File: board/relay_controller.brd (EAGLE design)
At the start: 70 x 50 mm, 53 parts, among them IC1 STM32F103C8T, IC3 AT24C, X1 RJ45-8L21-S, X2 RJ45-8L21-S

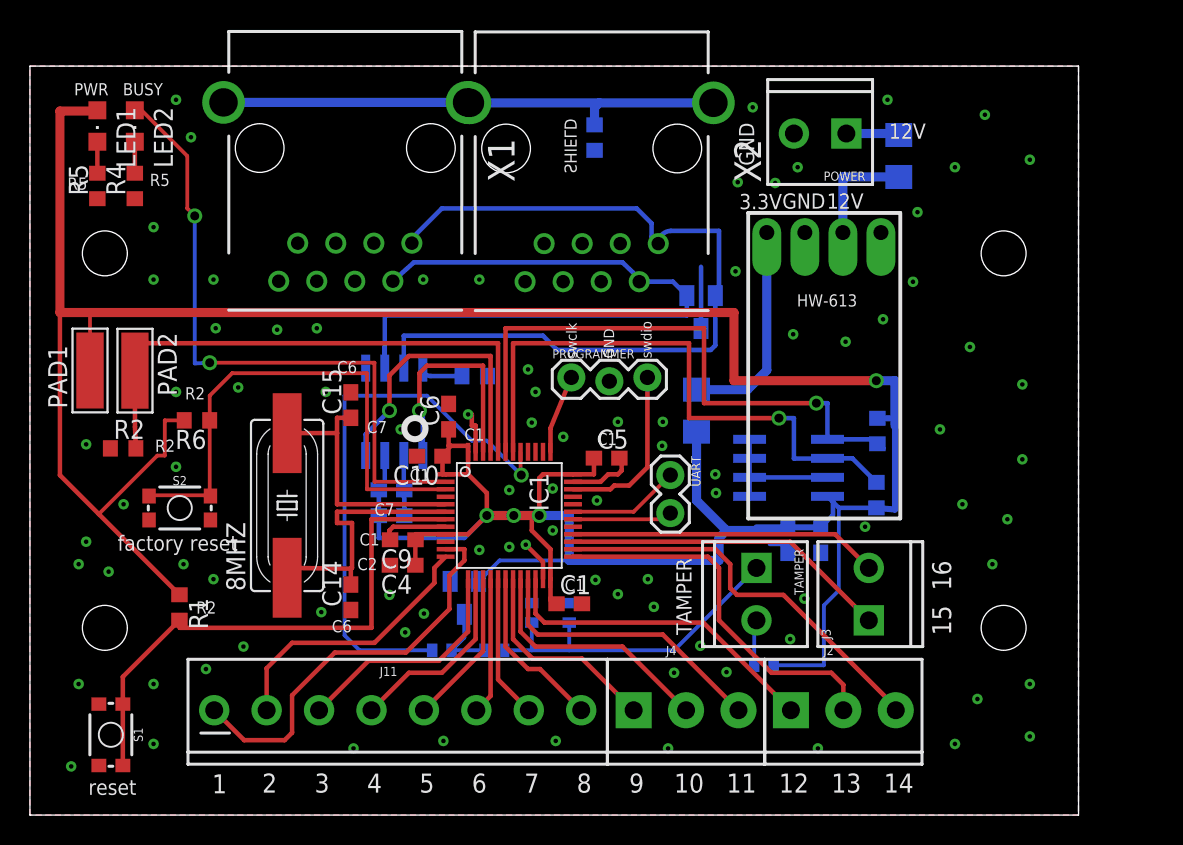
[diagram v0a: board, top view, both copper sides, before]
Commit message: add 3.3v output for relay board
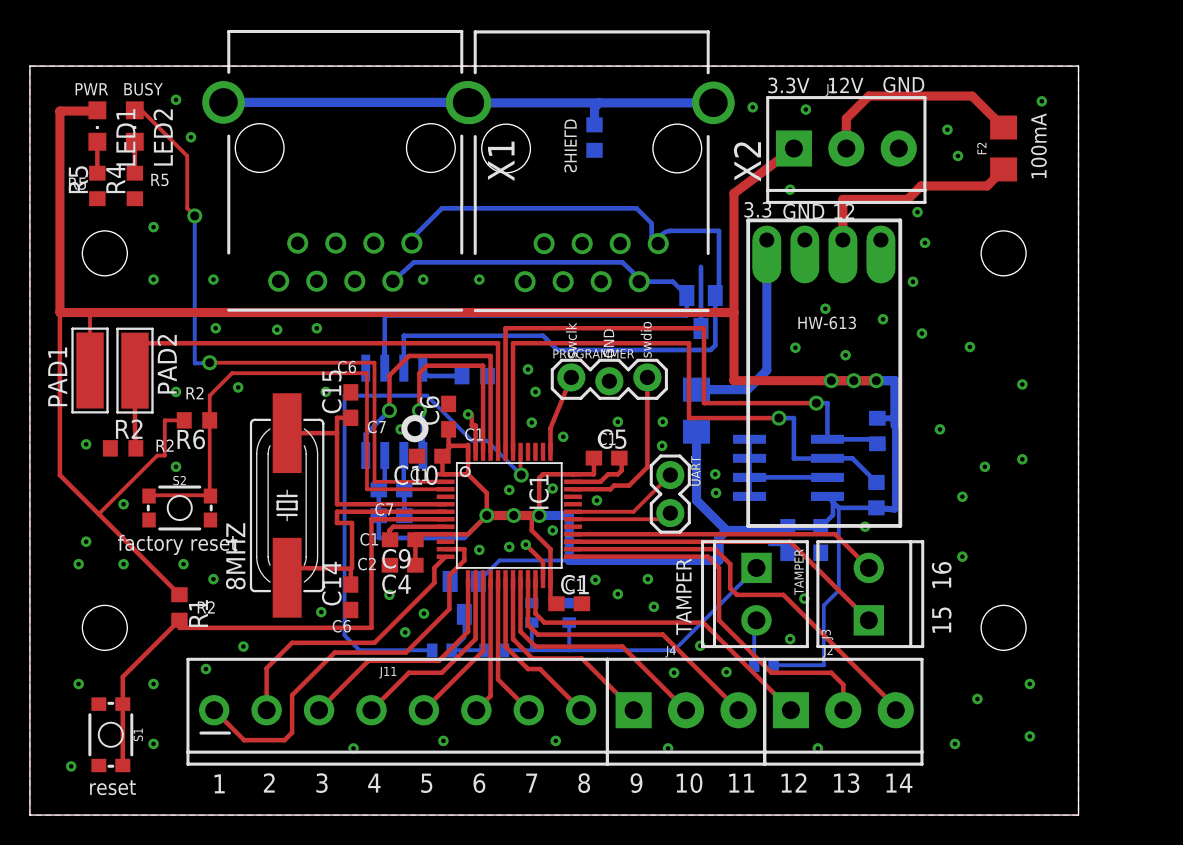
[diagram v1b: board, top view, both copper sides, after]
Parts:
- removed POWER: (no value), SparkFun-Connectors:SCREWTERMINAL-3.5MM-2
- added J1: (no value), SparkFun-Connectors:SCREWTERMINAL-3.5MM-3
- moved F2 7.02 mm to (65.0, 44.5), flipped to the top
- moved U$1 0.50 mm to (53.0, 29.5)
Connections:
- net +3V3: now also J1.1
- net GND: now also J1.3; no longer POWER.2
- net N$4: now also J1.2; no longer POWER.1
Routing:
- net +3V3: track 239.8 -> 255.8 mm, vias 4 -> 6
- net N$4: track 3.60 -> 14.0 mm
- net +12V: track 7.44 -> 14.3 mm
- net N$3: track 14.4 -> 13.9 mm
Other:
- board text added: "100mA"
- board text added: "3.3"
- board text added: "relay controller 2020.06.07 v1.1"
- board text removed: "2020.05.07 v1.0"
- board text removed: "50mA"

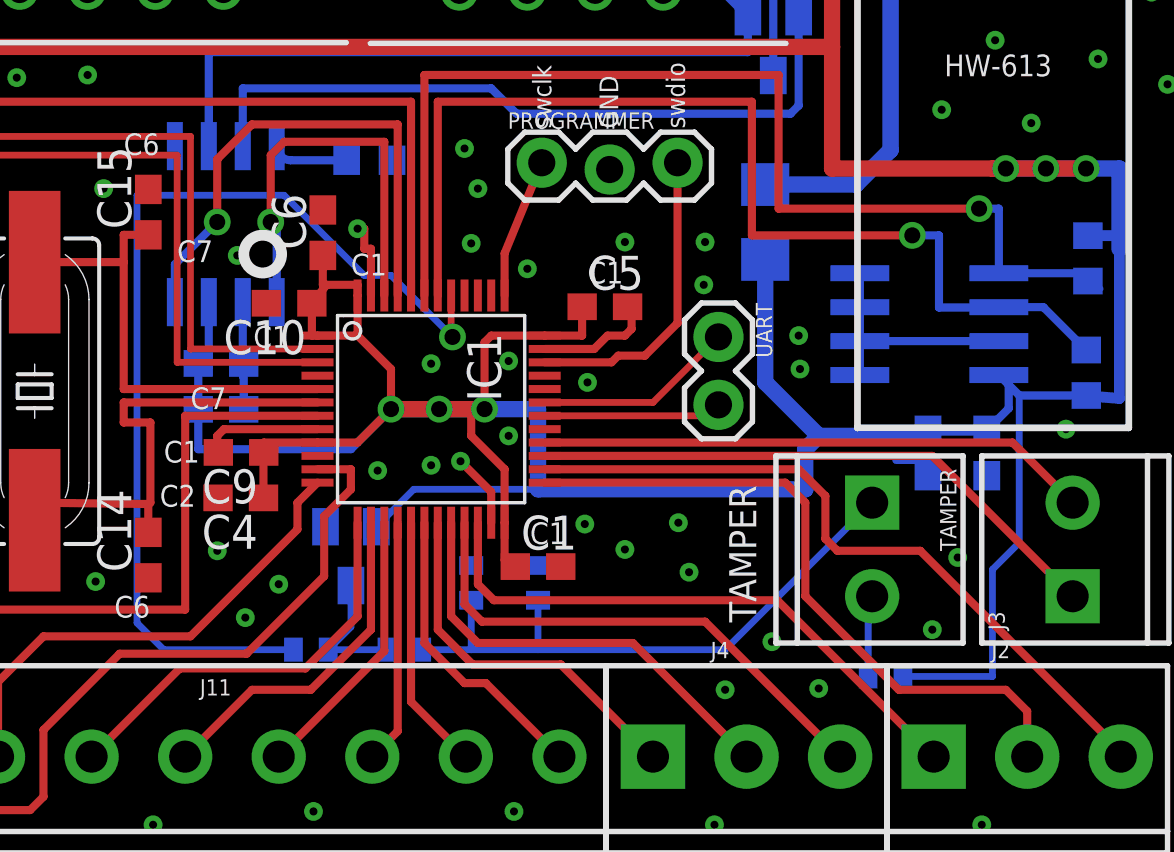
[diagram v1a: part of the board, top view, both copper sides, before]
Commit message: add 3.3v output
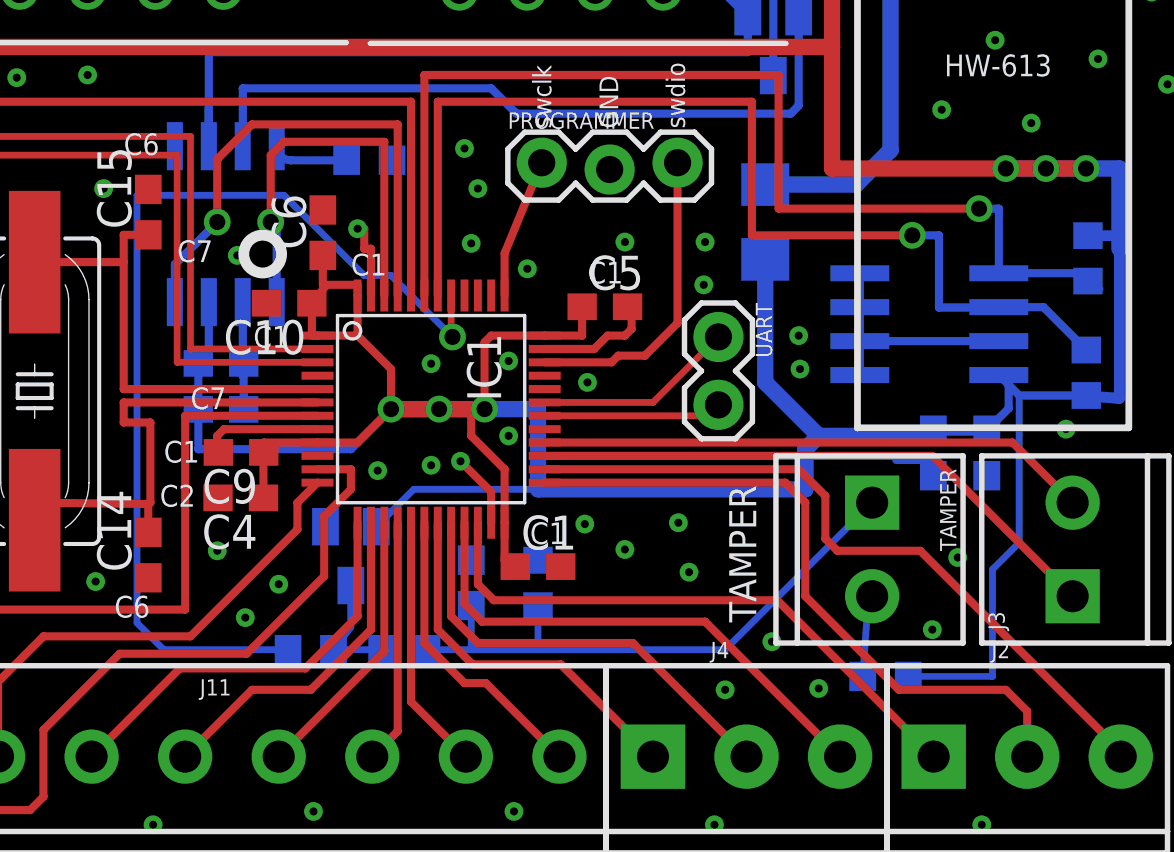
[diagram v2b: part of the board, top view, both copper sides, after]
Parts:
- C11: device eagle-ltspice:C0402 -> eagle-ltspice:C0603
- R59, R60, R61, R62: device rcl:R0402 -> rcl:R0603
- moved C2 0.20 mm to (50.8, 18.4)
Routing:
- net N$5: track 22.8 -> 22.2 mm
- net ASDASD: track 4.95 -> 4.42 mm
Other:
- board text added: "C13"
- board text removed: "C9"
- board text removed: "R16"
- board text removed: "R17"

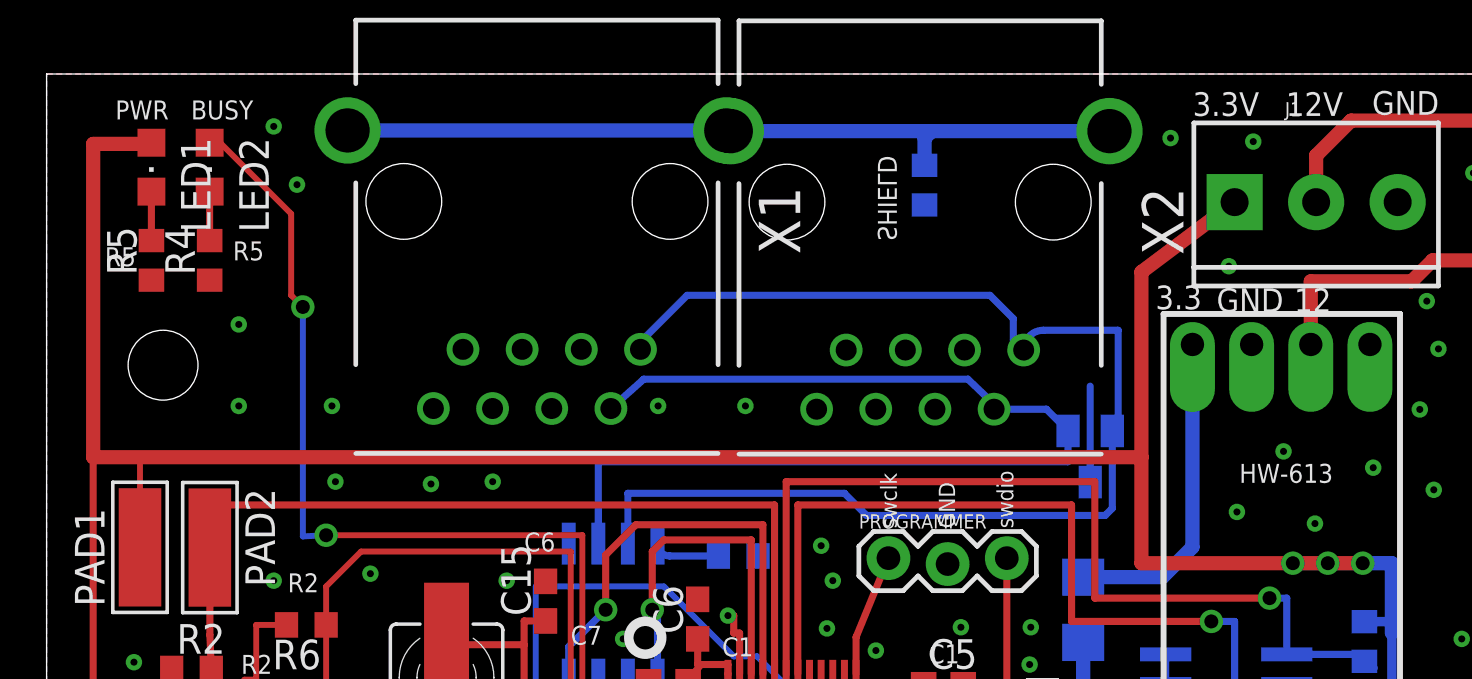
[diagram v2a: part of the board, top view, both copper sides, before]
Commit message: power over can
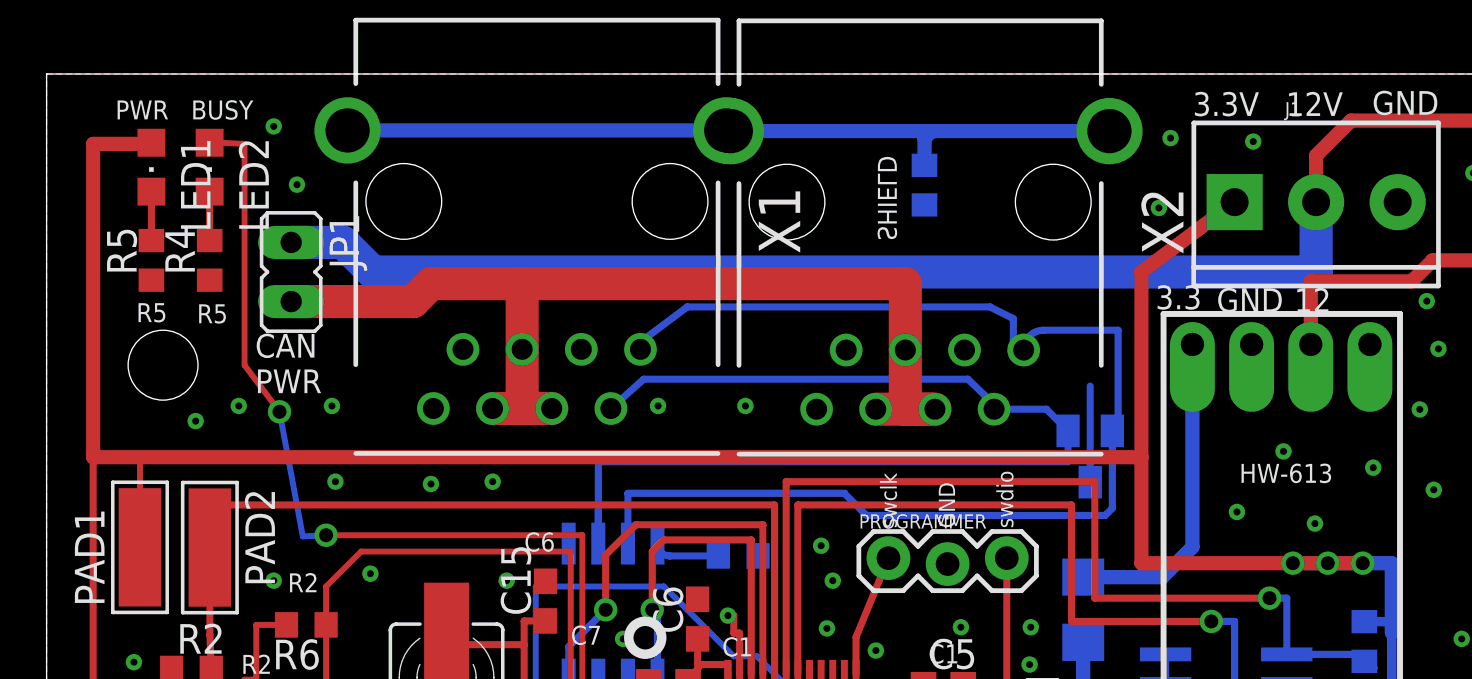
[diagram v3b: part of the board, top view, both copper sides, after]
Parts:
- added JP1: (no value), jumper:JP1
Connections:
- removed net N$4: F2.2, J1.2
- new net PRE_FUSE_12V: F2.2, J1.2, JP1.1
- new net RJ45_12V: JP1.2, X1.4, X1.5, X1.6, X2.4, X2.5, X2.6
- net GND: now also X1.8, X2.8
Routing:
- net PRE_FUSE_12V: track 0.00 -> 61.5 mm
- net RJ45_12V: track 0.00 -> 45.1 mm
- net N$4: track 14.0 -> 0.00 mm
- net CAN_H: track 54.7 -> 54.1 mm
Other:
- board text added: "CAN PWR"
- board text added: "relay controller 2020.06.12 v1.1"
- board text removed: "relay controller 2020.06.07 v1.1"

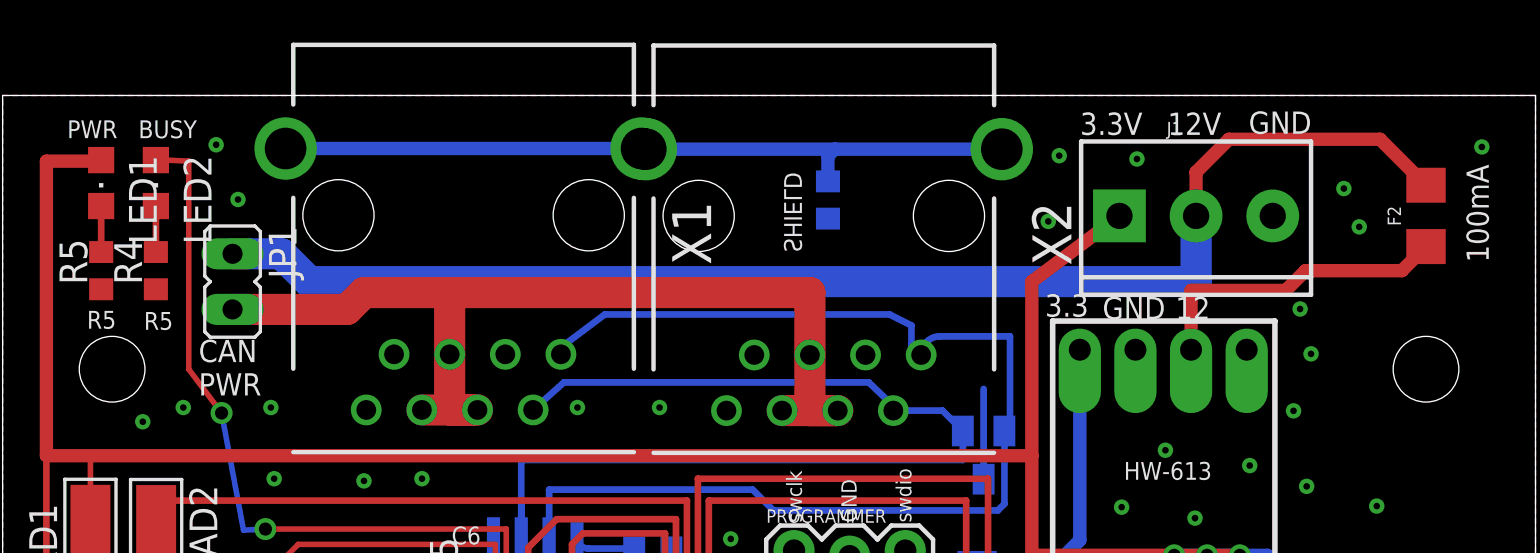
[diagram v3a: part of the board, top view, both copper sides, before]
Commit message: add varistor
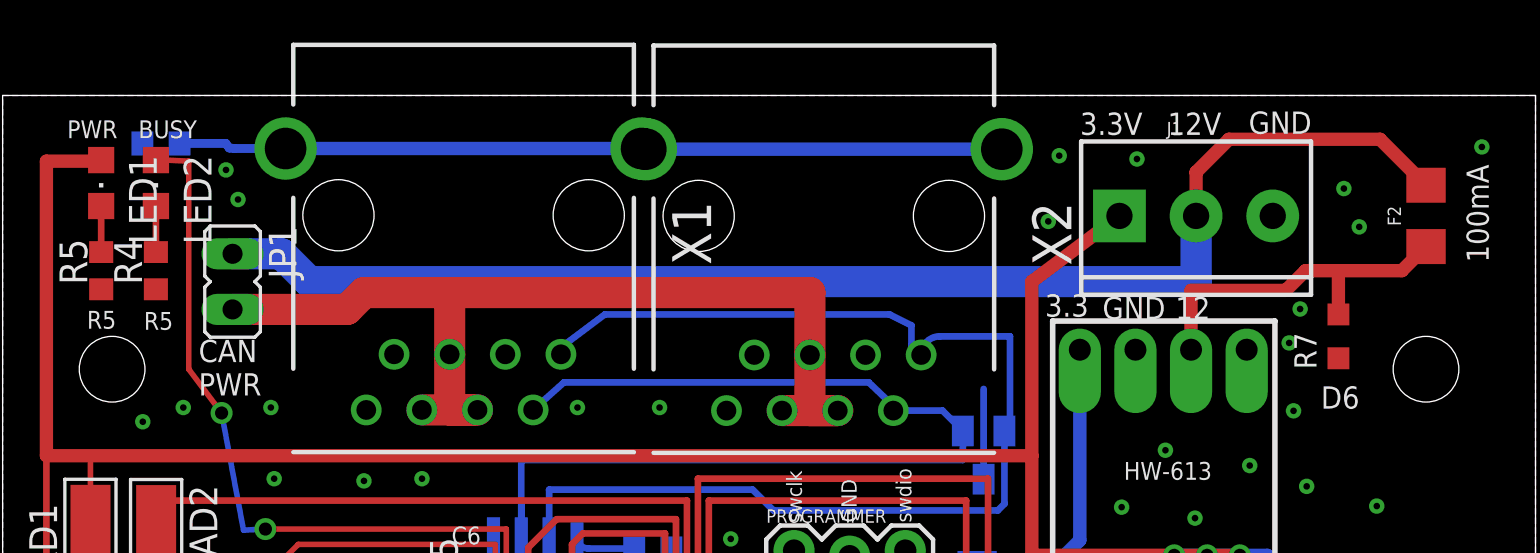
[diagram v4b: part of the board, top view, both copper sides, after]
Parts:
- added R7: VARISTORCN0603, varistor:CT/CN0603
- moved R25 30.6 mm to (7.23, 47.8), turned to 0 degrees
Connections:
- net +12V: now also R7.2
- net GND: now also R7.1
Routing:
- net N$20: track 34.3 -> 37.7 mm
- net +12V: track 14.3 -> 16.3 mm
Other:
- board text added: "D6"
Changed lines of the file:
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@@
 <text x="3.85" y="39.35" size="0.8128" layer="121">R5</text>
 <text x="6.45" y="39.3" size="0.8128" layer="121">R5</text>
-<text x="36.5" y="46.5" size="0.8128" layer="121" rot="MR270">SHIELD</text>
+<text x="1.5" y="48" size="0.8128" layer="122" rot="MR180">SHIELD</text>
 <text x="20.5" y="29.5" size="0.8128" layer="121">C6</text>
 <text x="20.15" y="12.2" size="0.8128" layer="121">C6</text>
@@
 <text x="8.95" y="36.3" size="1.016" layer="121">CAN
 PWR</text>
+<text x="60.2" y="35.7" size="1.016" layer="121">D6</text>
 </plain>
 <attributes>
@@
 </element>
 <element name="R24" library="rcl" package="R0603" value="0" x="29.69" y="29.31" rot="MR180"/>
-<element name="R25" library="rcl" package="R0603" value="10k" x="37.69" y="45.23" rot="MR270"/>
+<element name="R25" library="rcl" package="R0603" value="10k" x="7.23" y="47.81" rot="MR0"/>
 <element name="D5" library="diode" package="SOT23" value="PESD1CAN" x="44.8" y="33.58" rot="MR180"/>
 <element name="R27" library="rcl" package="R0603" value="4k7" x="56.57" y="25.64" rot="MR90"/>
@@
 </element>
 <element name="JP1" library="jumper" package="JP1" value="" x="10.5" y="41.5" rot="R180"/>
+<element name="R7" library="varistor" package="CT/CN0603" value="VARISTORCN0603" x="61" y="39" rot="R90"/>
 </elements>
 <signals>
@@
 <via x="8.25" y="35.75" extent="1-16" drill="0.3"/>
 <via x="6.4" y="35.1" extent="1-16" drill="0.3"/>
-<via x="9.75" y="47.75" extent="1-16" drill="0.3"/>
+<via x="10.2" y="46.6" extent="1-16" drill="0.3"/>
 <via x="10.75" y="45.25" extent="1-16" drill="0.3"/>
 <via x="12.25" y="35.75" extent="1-16" drill="0.3"/>
 <via x="53.1" y="33.8" extent="1-16" drill="0.3"/>
-<via x="59.75" y="38.2" extent="1-16" drill="0.3"/>
+<via x="58.75" y="38.7" extent="1-16" drill="0.3"/>
 <via x="47.75" y="44.25" extent="1-16" drill="0.3"/>
 <via x="48.25" y="47.25" extent="1-16" drill="0.3"/>
@@
 <contactref element="X2" pad="8"/>
 <contactref element="X1" pad="8"/>
-<wire x1="37.69" y1="44.38" x2="39.405" y2="38.15" width="0" layer="19" extent="16-16"/>
+<contactref element="R7" pad="1"/>
 </signal>
 <signal name="+3V3">
@@
 <wire x1="54.27" y1="41.1" x2="58.6" y2="41.1" width="0.6096" layer="1"/>
 <wire x1="58.6" y1="41.1" x2="59.5" y2="42" width="0.6096" layer="1"/>
-<wire x1="59.5" y1="42" x2="63.9" y2="42" width="0.6096" layer="1"/>
+<wire x1="59.5" y1="42" x2="61" y2="42" width="0.6096" layer="1"/>
+<wire x1="61" y1="42" x2="63.9" y2="42" width="0.6096" layer="1"/>
 <wire x1="63.9" y1="42" x2="65" y2="43.1" width="0.6096" layer="1"/>
+<contactref element="R7" pad="2"/>
+<wire x1="61" y1="40" x2="61" y2="42" width="0.6096" layer="1"/>
 </signal>
 <signal name="N$1">
@@
 <wire x1="29.178" y1="47.578" x2="29.372" y2="47.578" width="0.6096" layer="16"/>
 <wire x1="29.372" y1="47.578" x2="29.372" y2="47.548" width="0.6096" layer="16"/>
-<wire x1="29.372" y1="47.548" x2="38" y2="47.548" width="0.6096" layer="16"/>
-<wire x1="38" y1="47.548" x2="45.628" y2="47.548" width="0.6096" layer="16"/>
-<wire x1="37.69" y1="46.08" x2="37.69" y2="47.238" width="0.6096" layer="16"/>
-<wire x1="37.69" y1="47.238" x2="38" y2="47.548" width="0.6096" layer="16"/>
+<wire x1="29.372" y1="47.548" x2="45.628" y2="47.548" width="0.6096" layer="16"/>
+<wire x1="8.08" y1="47.81" x2="10.19" y2="47.81" width="0.4064" layer="16"/>
+<wire x1="10.19" y1="47.81" x2="10.35" y2="47.6" width="0.4064" layer="16"/>
+<wire x1="10.35" y1="47.6" x2="10.578" y2="47.578" width="0.4064" layer="16"/>
+<wire x1="10.578" y1="47.578" x2="12.922" y2="47.578" width="0.4064" layer="16"/>
 </signal>
 <signal name="I2C1_SDA">
